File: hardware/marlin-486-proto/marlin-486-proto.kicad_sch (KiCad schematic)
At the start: 16 parts, among them J1 Conn_01x03, U1 AM486DX

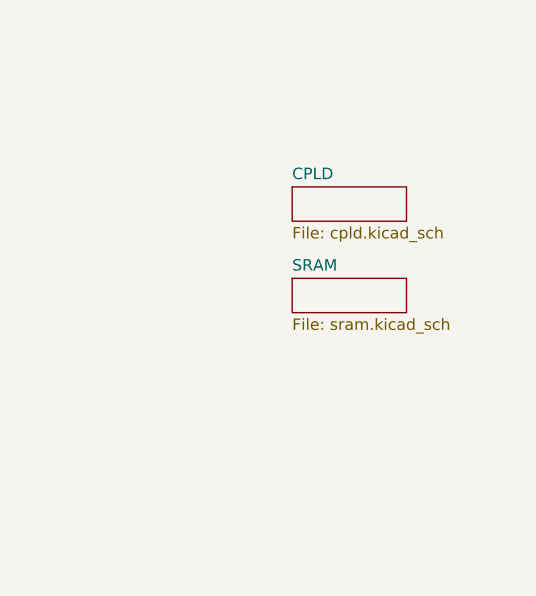
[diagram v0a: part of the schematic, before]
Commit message: Add 16C550 symbol
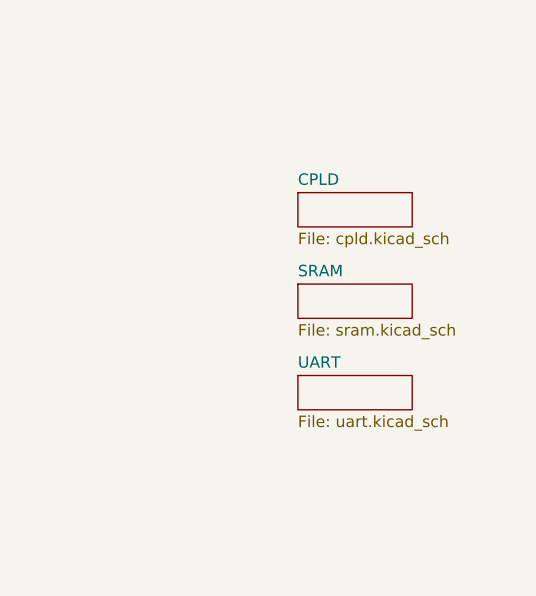
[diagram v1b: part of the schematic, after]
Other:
- added sheet UART (uart.kicad_sch)
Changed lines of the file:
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@@
 	)
 	(sheet
-		(at 227.33 66.04)
+		(at 227.965 66.675)
 		(size 12.7 3.81)
 		(fields_autoplaced yes)
@@
 		)
 		(property "Sheetname" "CPLD"
-			(at 227.33 65.3284 0)
+			(at 227.965 65.9634 0)
 			(effects
 				(font
@@
 		)
 		(property "Sheetfile" "cpld.kicad_sch"
-			(at 227.33 70.4346 0)
+			(at 227.965 71.0696 0)
 			(effects
 				(font
@@
 	)
 	(sheet
-		(at 227.33 76.2)
+		(at 227.965 76.835)
 		(size 12.7 3.81)
 		(fields_autoplaced yes)
@@
 		)
 		(property "Sheetname" "SRAM"
-			(at 227.33 75.4884 0)
+			(at 227.965 76.1234 0)
 			(effects
 				(font
@@
 		)
 		(property "Sheetfile" "sram.kicad_sch"
-			(at 227.33 80.5946 0)
+			(at 227.965 81.2296 0)
 			(effects
 				(font
@@
 				)
 			)
+		)
+	)
+	(sheet
+		(at 227.965 86.995)
+		(size 12.7 3.81)
+		(fields_autoplaced yes)
+		(stroke
+			(width 0.1524)
+			(type solid)
+		)
+		(fill
+			(color 0 0 0 0.0000)
+		)
+		(property "Sheetname" "UART"
+			(at 227.965 86.2834 0)
+			(effects
+				(font
+					(size 1.27 1.27)
+				)
+				(justify left bottom)
+			)
+		)
+		(property "Sheetfile" "uart.kicad_sch"
+			(at 227.965 91.3896 0)
+			(effects
+				(font
+					(size 1.27 1.27)
+				)
+				(justify left top)
+			)
+		)
+		(instances
+			(project "marlin-486-proto"
+				(path "/a6a50ac5-2956-43ae-b999-06077790d4e0"
+					(page "4")
+				)
+			)
